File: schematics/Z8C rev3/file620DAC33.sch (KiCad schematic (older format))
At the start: 35 parts, among them J1 Barrel_Jack, SW1 SW_DPST

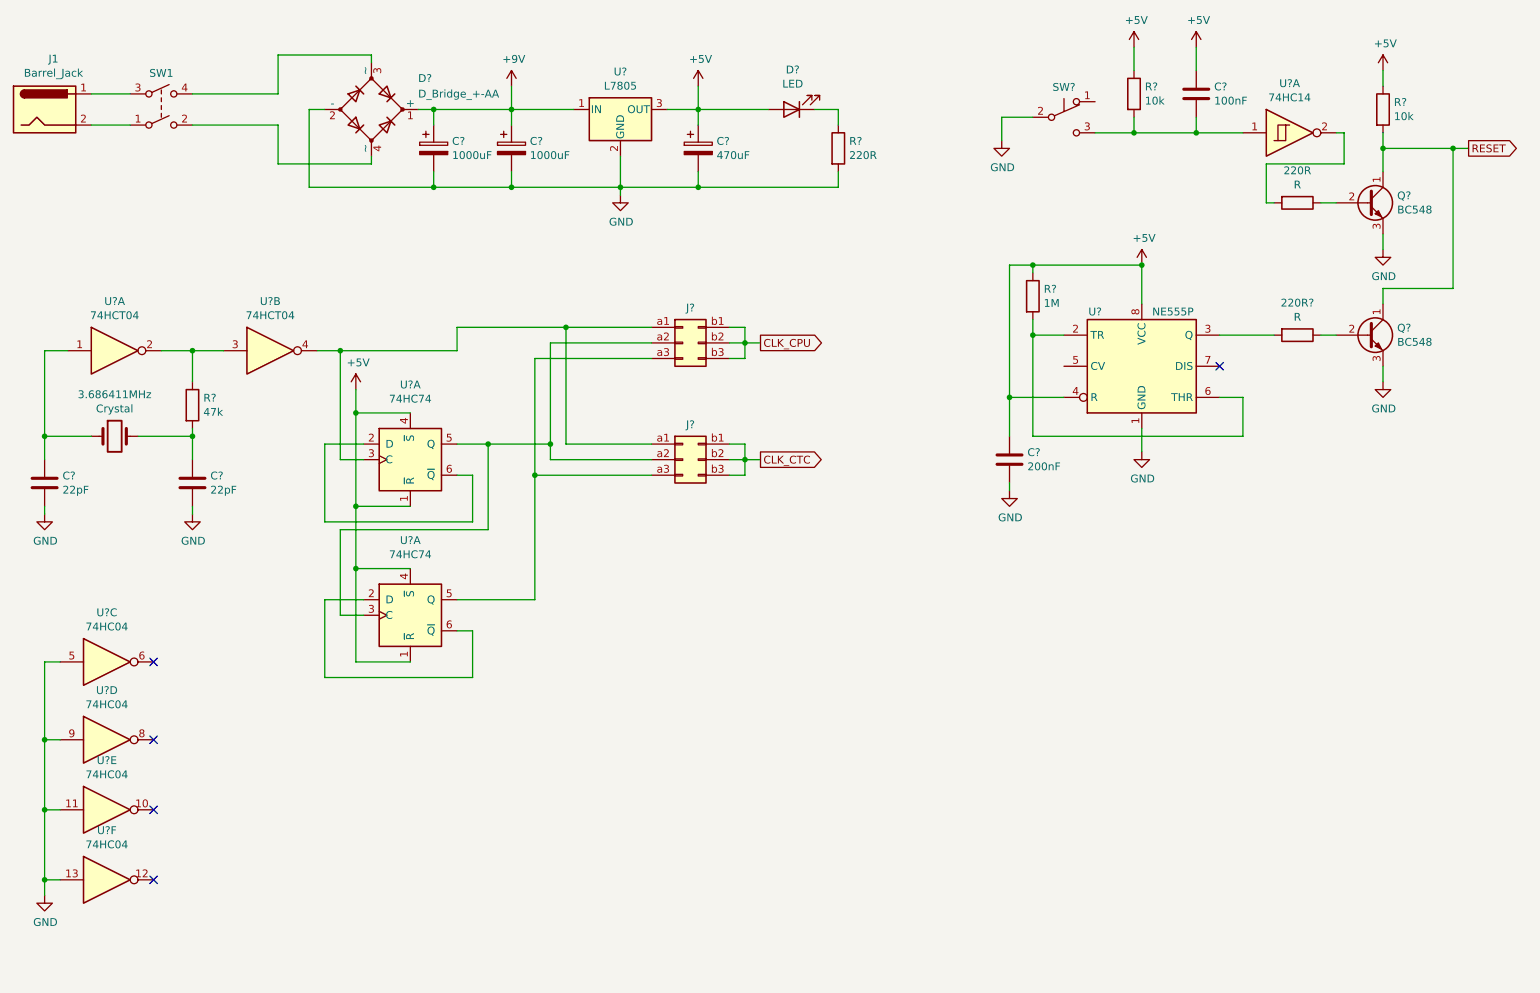
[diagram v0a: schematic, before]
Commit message: working on sound
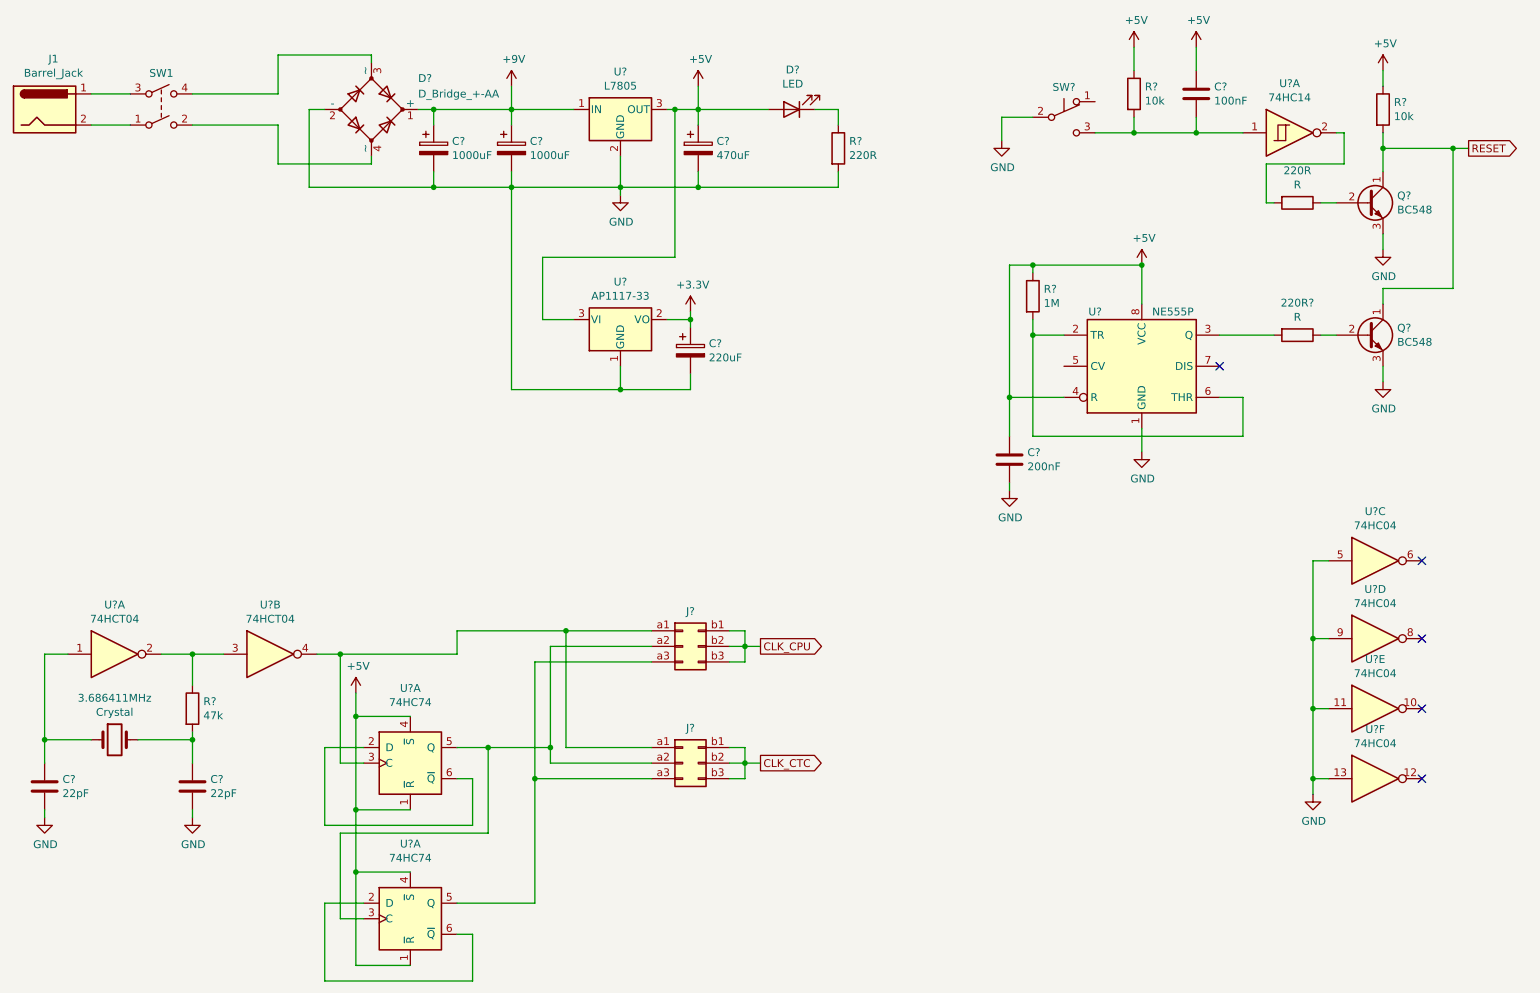
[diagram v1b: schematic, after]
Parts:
- added C?: 220uF, symbol Device:CP
- added U?: AP1117-33, Package_TO_SOT_SMD:SOT-223-3_TabPin2, symbol Regulator_Linear:AP1117-33
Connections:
- net +5V: now also U?.3 (VI)
- net GND: now also C?.2, U?.1 (GND)
- new net +3V3: C?.1, U?.2 (VO)
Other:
- moved on the sheet: 3.686411MHz, C?, J?, R?, U?A, U?B, U?C, U?D, U?E, U?F

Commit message: added bank switching, apu, dma and IRQ logic. Misc. improvements
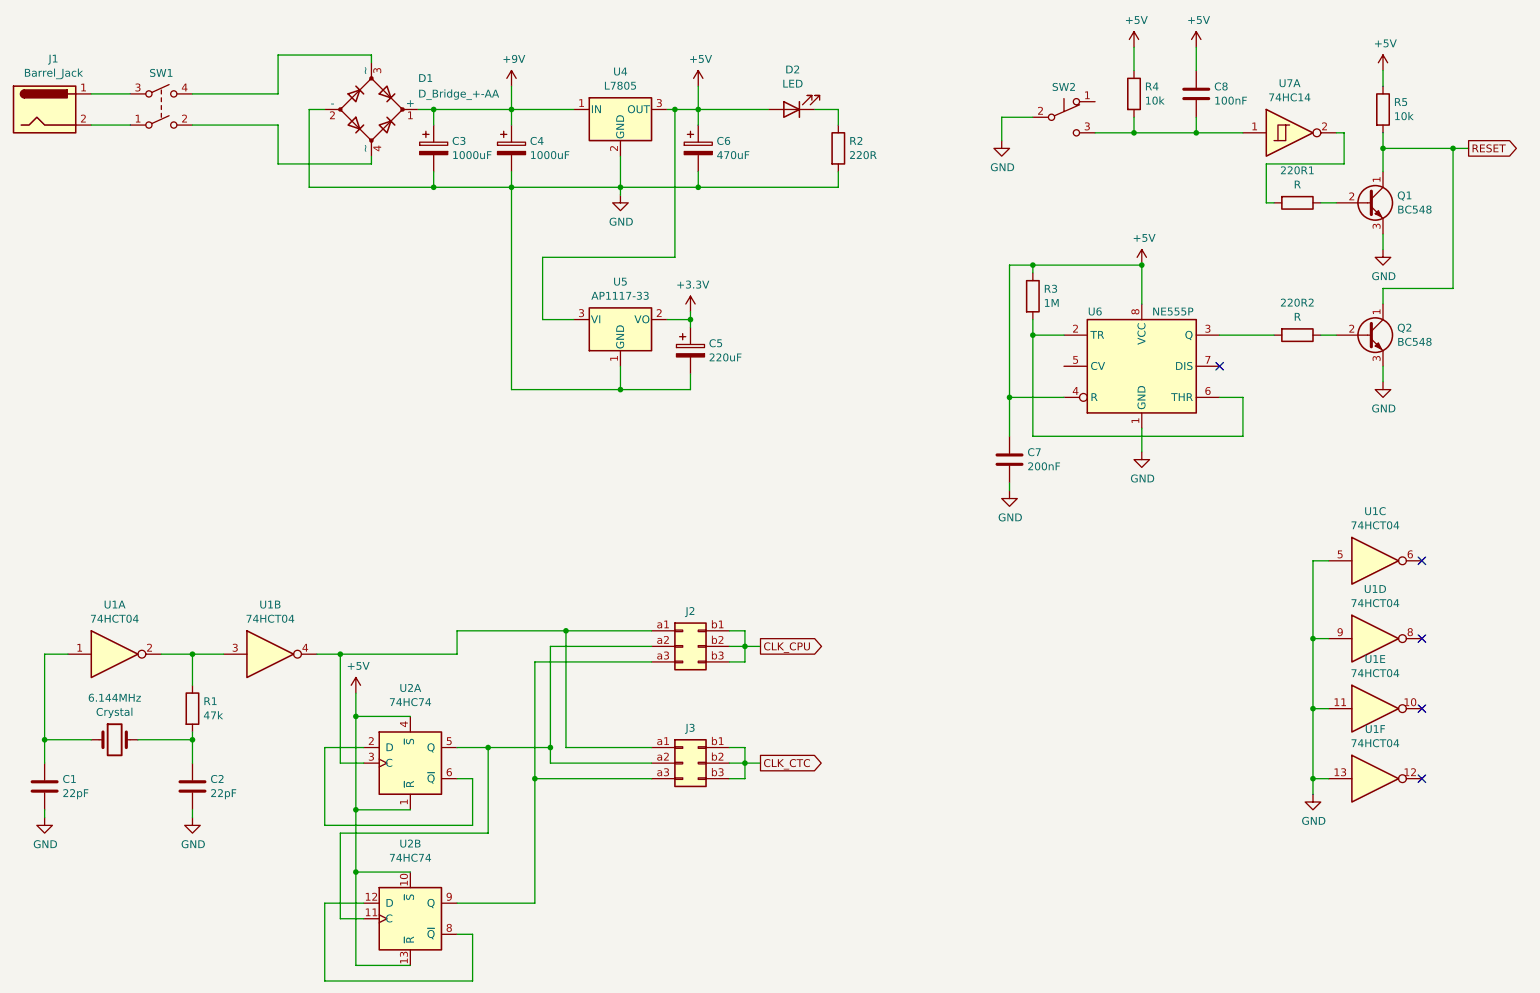
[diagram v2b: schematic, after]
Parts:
- removed U?: 74HC74, symbol 74xx:74HC74
- removed U? (x4): 74HC04, symbol 74xx:74HC04
- added unit 3 of U1
- added unit 4 of U1
- added unit 5 of U1
- added unit 6 of U1
- added unit 2 of U2
- J2, J3: renamed from J?; footprint (none) -> Connector_PinHeader_2.54mm:PinHeader_2x03_P2.54mm_Vertical
- U1, U2, U7: renamed from U?; footprint (none) -> Package_DIP:DIP-14_W7.62mm_LongPads
- gave numbers to parts that had none: 22
- renumbered 220R to 220R1, 3.686411MHz to 6.144MHz
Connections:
- net +5V: now also U2.10 (~S), U2.13 (~R)
- net GND: now also U1.11, U1.13, U1.5, U1.9
- net at J2.a2 (Pin_a2), J3.a2 (Pin_a2), U2.5 (Q): now also U2.11 (C)
- net at J2.a3 (Pin_a3), J3.a3 (Pin_a3): now also U2.9 (Q)
- new net: U2.12 (D), U2.8 (~Q)
